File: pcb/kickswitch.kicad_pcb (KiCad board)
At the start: 2 copper layers, 54.8 x 63.9 mm, 13 parts, among them J2 2x4hdr, SW1 SW_RST, U1 SN74LVC1G08, U2 SN74LVC1G32, U3 ATMEGA328P-PU, U4 KS Sock, U5 M27C160, Y1 16MHz

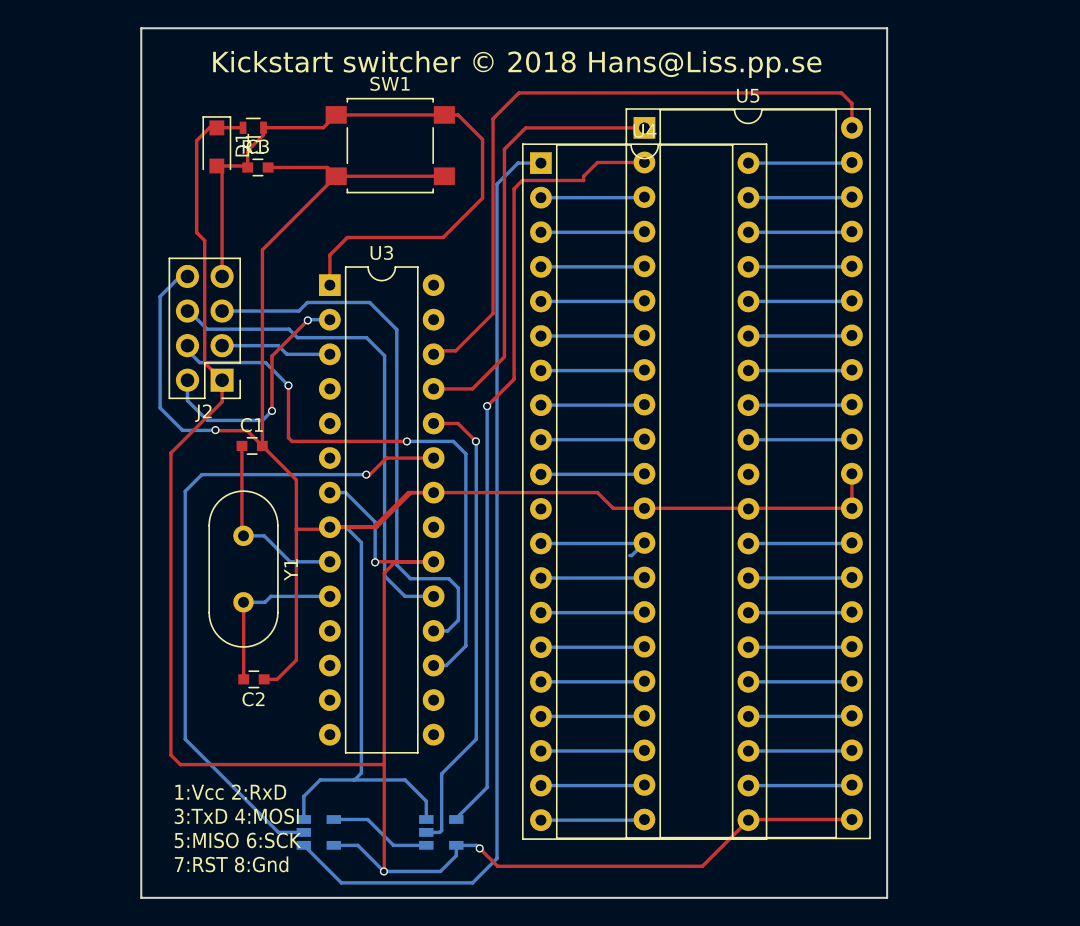
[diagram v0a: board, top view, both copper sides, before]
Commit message: Added many more I/O pins Removed reset button Added resistor nets for Address line pullups Added ground plane
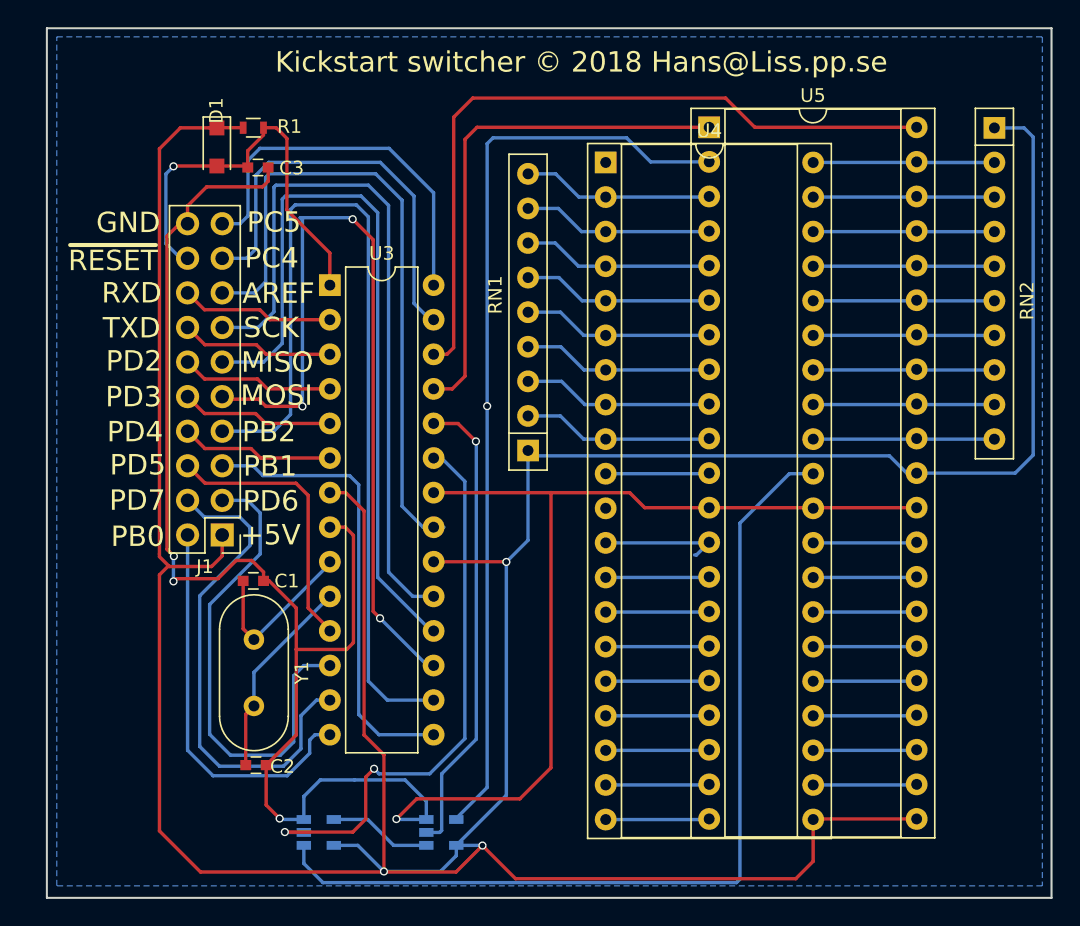
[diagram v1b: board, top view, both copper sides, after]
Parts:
- removed J2: 2x4hdr, Pin_Headers:Pin_Header_Straight_2x04_Pitch2.54mm
- removed SW1: SW_RST, Buttons_Switches_SMD:SW_SPST_B3S-1000
- added J1: J1, Pin_Headers:Pin_Header_Straight_2x10_Pitch2.54mm, F.Cu at (89.4, 130.3)
- added RN1: 4k7, Resistors_THT:R_Array_SIP9, F.Cu at (111.8, 124.1)
- added RN2: 4k7, Resistors_THT:R_Array_SIP10, F.Cu at (146.1, 100.4)
- U4: value KS Sock -> MC23C4100_socket
- moved C1 9.91 mm to (91.6, 133.7)
- moved Y1 7.65 mm to (91.7, 138.0)
- moved C2 6.30 mm to (91.8, 147.2)
- moved U4 4.76 mm to (117.5, 103.0)
- moved U5 4.76 mm to (125.1, 100.4)
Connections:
- net /A17out renamed Net-(U2-Pad4)
- net /RESET renamed /~RESET
- U3 pad 11: Net-(U3-Pad11) -> /PD5
- U3 pad 12: Net-(U3-Pad12) -> /PD6
- U3 pad 13: Net-(U3-Pad13) -> /PD7
- U3 pad 14: Net-(U3-Pad14) -> /PB0
- U3 pad 15: Net-(U3-Pad15) -> /PB1
- U3 pad 16: Net-(U3-Pad16) -> /PB2
- U3 pad 21: Net-(U3-Pad21) -> /AREF
- U3 pad 27: Net-(U3-Pad27) -> /PC4
- U3 pad 28: Net-(U3-Pad28) -> /PC5
- U3 pad 4: Net-(U3-Pad4) -> /PD2
- U3 pad 5: Net-(U3-Pad5) -> /PD3
- U3 pad 6: Net-(U3-Pad6) -> /PD4
- U4 pad 1: /A17in -> Net-(U4-Pad1)
- U4 pad 31: Net-(U4-Pad31) -> /A17in
- U5 pad 32: /Gnd -> /Vcc
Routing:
- net /Vcc: track 147.3 -> 270.8 mm
- net /PB2: track 0.00 -> 66.3 mm
- net /AREF: track 0.00 -> 48.3 mm
- net /PD7: track 0.00 -> 36.6 mm
- net /PD6: track 0.00 -> 36.0 mm
- net /PB1: track 0.00 -> 33.6 mm
- net /PC4: track 0.00 -> 31.4 mm
- net /PB0: track 0.00 -> 28.9 mm
- net /PC5: track 0.00 -> 28.3 mm
- net /PD5: track 0.00 -> 20.4 mm
- net /~RESET: track 50.5 -> 31.6 mm, vias 0 -> 1
- net /SCK: track 36.3 -> 53.5 mm
- net /MOSI: track 43.3 -> 59.5 mm, vias 2 -> 3
- net /MISO: track 40.9 -> 55.7 mm
- net /PD3: track 0.00 -> 11.3 mm
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- added copper zone on B.Cu, net /Gnd
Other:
- board size 54.8 x 63.9 mm -> 73.8 x 63.9 mm
- board text added: "+5V"
- board text added: "AREF"
- board text added: "GND"
- board text added: "MISO"
- board text added: "MOSI"
- board text added: "PB0"
- board text added: "PB1"
- board text added: "PB2"
- board text added: "PC4"
- board text added: "PC5"
- board text added: "PD2"
- board text added: "PD3"
- board text added: "PD4"
- board text added: "PD5"
- board text added: "PD6"
- board text added: "PD7"
- board text added: "RXD"
- board text added: "SCK"
- board text added: "TXD"
- board text added: "~RESET"
- board text removed: "1:Vcc 2:RxD 3:TxD 4:MOSI 5:MISO 6:SCK 7:RST 8:Gnd"

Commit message: Upgraded to latest KiCAD. Eliminated encoder. Eliminated switch and added /RSTOUT input line instead. Added jumper for pin 1/31 "Oops" fix. Updated README.md.
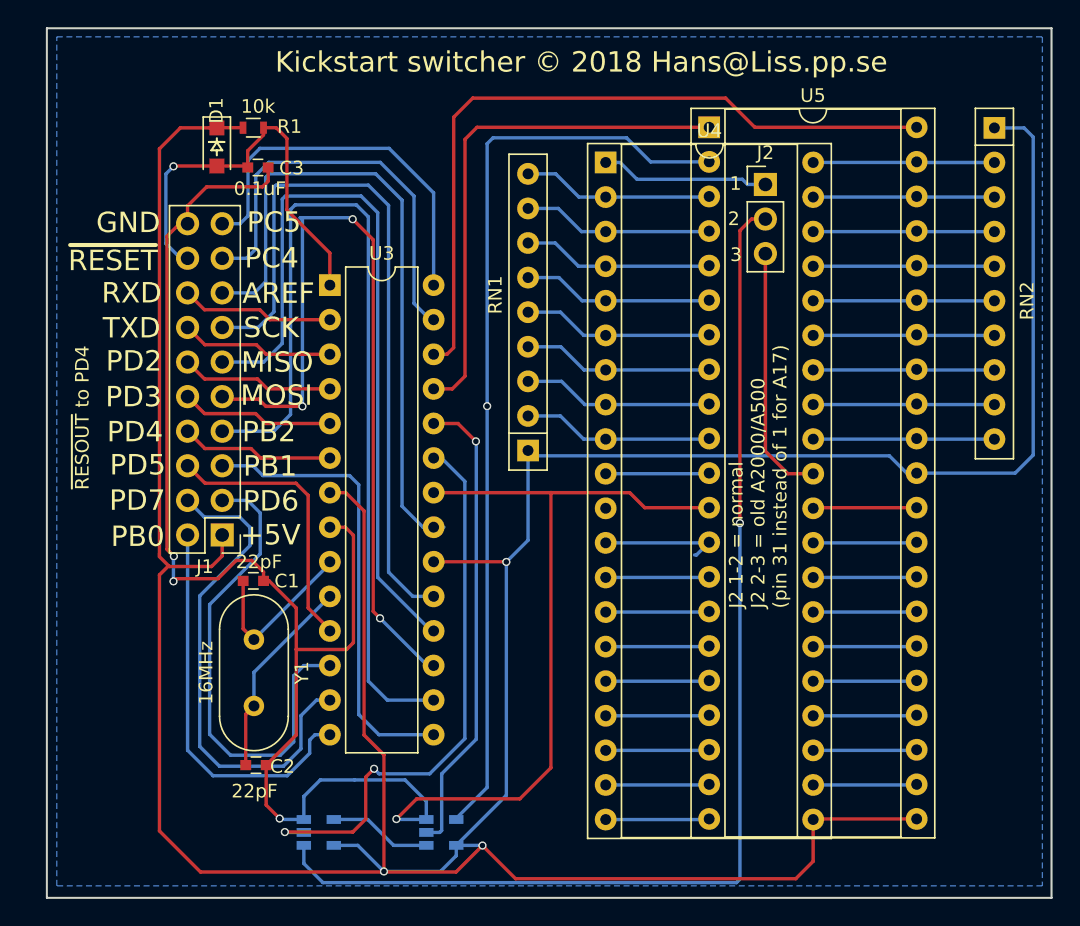
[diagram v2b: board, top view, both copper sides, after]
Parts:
- added J2: Conn_01x03, Pin_Headers:Pin_Header_Straight_1x03_Pitch2.54mm, F.Cu at (129.2, 104.6)
- J1: value J1 -> Conn_02x10_Odd_Even
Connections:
- U4 pad 11: Net-(U4-Pad11) -> (no net)
- U4 pad 31: /A17in -> Net-(J2-Pad3)
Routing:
- net Net-(J2-Pad3): track 0.00 -> 18.7 mm
- net /A17in: track 67.1 -> 83.9 mm, vias 0 -> 1
- net Net-(J2-Pad1): track 0.00 -> 12.4 mm
- net /Gnd: track 165.4 -> 157.8 mm
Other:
- board text added: "0.1uF"
- board text added: "1"
- board text added: "10k"
- board text added: "16MHz"
- board text added: "2"
- board text added: "22pF"
- board text added: "3"
- board text added: "J2 1-2 = normal J2 2-3 = old A2000/A500 (pin 31 instead of 1 for A17)"
- board text added: "~RESOUT~ to PD4"
